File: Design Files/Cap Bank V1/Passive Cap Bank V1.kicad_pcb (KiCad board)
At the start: 2 copper layers, 75 x 125 mm, 47 parts, among them J1 XT30-Male, Q1 BC817-40, Q2 BC817-40, Q3 BC817-40, Q4 BC817-40, Q5 BC817-40, Q6 BC817-40, SW1 SW_Push_Open

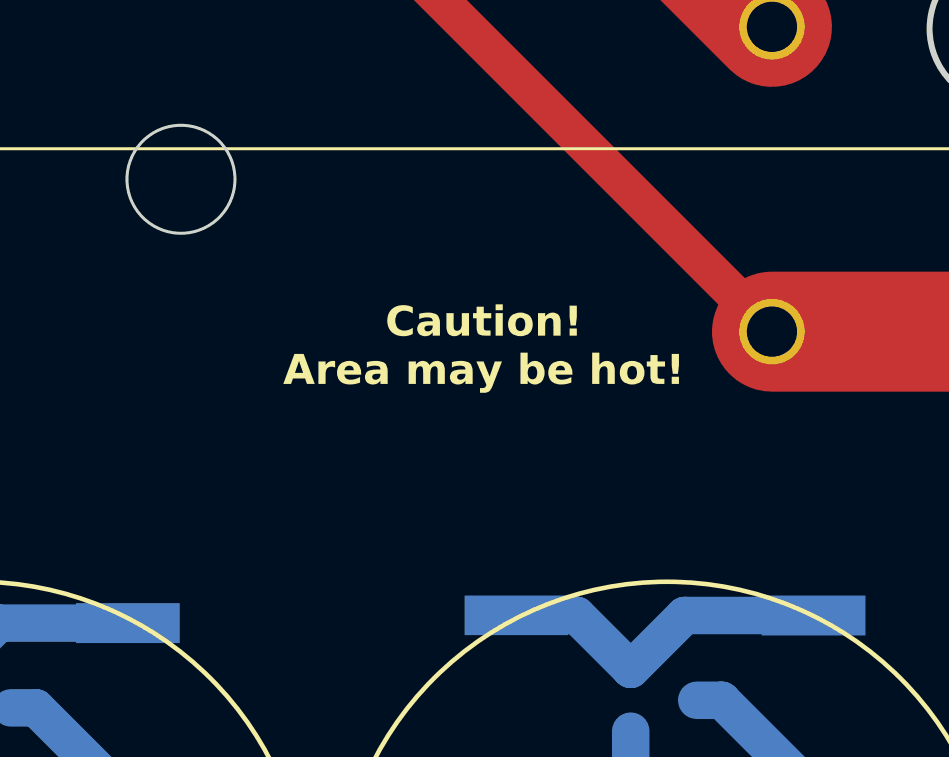
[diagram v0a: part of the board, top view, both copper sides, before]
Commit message: final cap bank changes
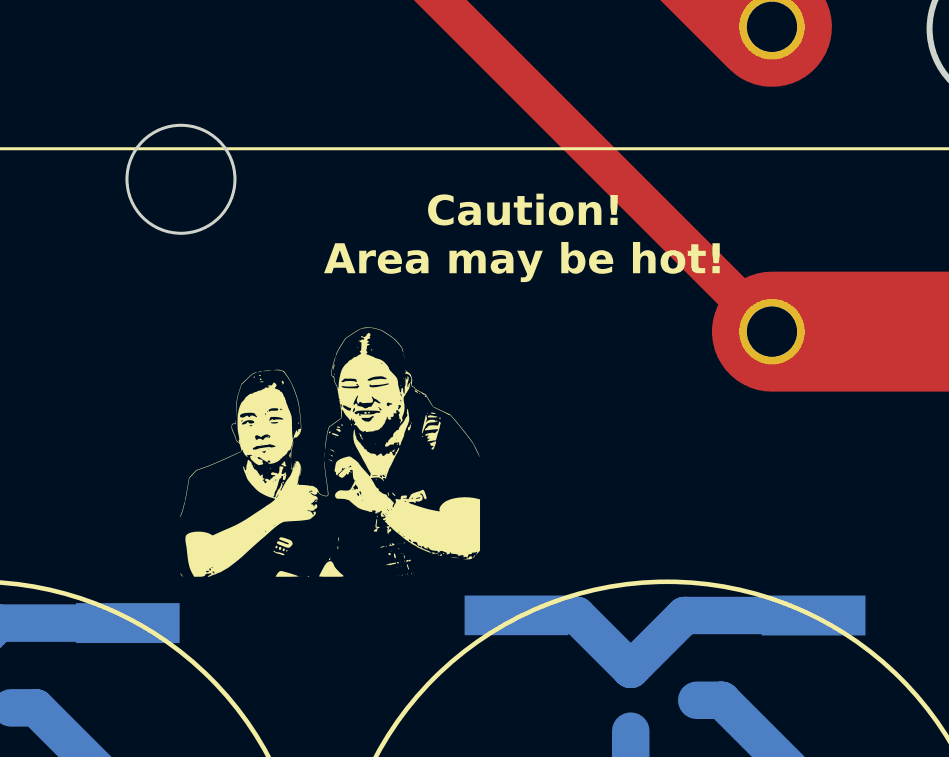
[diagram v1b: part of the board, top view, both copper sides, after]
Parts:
- added G***: LOGO, LOGO, F.Cu at (76.3, 108.9)
